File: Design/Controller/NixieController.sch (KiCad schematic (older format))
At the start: 25 parts, among them J1 Conn_01x12_Female, J2 Conn_01x12_Female, J3 Conn_01x12_Female, J4 Conn_01x12_Female, J5 Conn_01x12_Female, J6 Conn_01x12_Female, J7 Jack-DC, J8 Conn_01x02_Male, J9 Conn_01x06_Male, U1 ATtiny85-20SU, U10 74HC595, U11 74HC595, U12 74HC595, U2 DS1307Z+, U5 74HC595, U6 74HC595, U7 74HC595, U8 74HC595, U9 74HC595, Y1 32.768kHz

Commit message: Add part numbers to symbols in NixieController schematic for BOM
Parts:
- C7, C8: Digikey # (none) -> 1276-1007-6-ND; Manufacturer (none) -> SAMSUNG
- J7: Digikey # (none) -> 2092-KLDX-0202-A-ND; Manufacturer (none) -> KYCON
- R1, R2: Digikey # (none) -> 311-4.7KARDKR-ND; Manufacturer (none) -> YAGEO
- U1: Digikey # (none) -> ATTINY85-20SURDKR-ND; Manufacturer (none) -> MICROCHIP
- U10, U11, U12, U5, U6, U7, U8, U9: Digikey # (none) -> 1727-2821-6-ND; Manufacturer (none) -> NEXPERIA
- U2: Digikey # (none) -> DS1307Z+T&RDKR-ND; Manufacturer (none) -> MAXIM
- Y1: Digikey # (none) -> SER4103DKR-ND; Manufacturer (none) -> EPSON
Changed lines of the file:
@@
 F 1 "Jack-DC" H 2757 7184 50  0000 C CNN
 F 2 "Connector_BarrelJack:BarrelJack_Horizontal" H 2750 6910 50  0001 C CNN
-F 3 "~" H 2750 6910 50  0001 C CNN
+F 3 "KLDX-0202-A" H 2750 6910 50  0001 C CNN
+F 4 "2092-KLDX-0202-A-ND" H 2700 6950 50  0001 C CNN "Digikey #"
+F 5 "KYCON" H 2700 6950 50  0001 C CNN "Manufacturer"
 	1    2700 6950
 	1    0    0    -1
@@
 F 1 "ATtiny85-20SU" H 1171 1355 50  0000 R CNN
 F 2 "Package_SO:SOIC-8_5.275x5.275mm_P1.27mm" H 1700 1400 50  0001 C CIN
-F 3 "http://ww1.microchip.com/downloads/en/DeviceDoc/atmel-2586-avr-8-bit-microcontroller-attiny25-attiny45-attiny85_datasheet.pdf" H 1700 1400 50  0001 C CNN
+F 3 "ATTINY85-20SUR" H 1700 1400 50  0001 C CNN
+F 4 "ATTINY85-20SURDKR-ND" H 1700 1400 50  0001 C CNN "Digikey #"
+F 5 "MICROCHIP" H 1700 1400 50  0001 C CNN "Manufacturer"
 	1    1700 1400
 	1    0    0    -1
@@
 F 1 "74HC595" H 1750 3850 50  0000 C CNN
 F 2 "Package_SO:SOIC-16_3.9x9.9mm_P1.27mm" H 1550 3300 50  0001 C CNN
-F 3 "http://www.ti.com/lit/ds/symlink/sn74hc595.pdf" H 1550 3300 50  0001 C CNN
+F 3 "74HC595D,118" H 1550 3300 50  0001 C CNN
+F 4 "1727-2821-6-ND" H 1550 3300 50  0001 C CNN "Digikey #"
+F 5 "NEXPERIA" H 1550 3300 50  0001 C CNN "Manufacturer"
 	1    1550 3300
 	1    0    0    -1
@@
 F 1 "74HC595" H 3350 3850 50  0000 C CNN
 F 2 "Package_SO:SOIC-16_3.9x9.9mm_P1.27mm" H 3150 3300 50  0001 C CNN
-F 3 "http://www.ti.com/lit/ds/symlink/sn74hc595.pdf" H 3150 3300 50  0001 C CNN
+F 3 "74HC595D,118" H 3150 3300 50  0001 C CNN
+F 4 "1727-2821-6-ND" H 3150 3300 50  0001 C CNN "Digikey #"
+F 5 "NEXPERIA" H 3150 3300 50  0001 C CNN "Manufacturer"
 	1    3150 3300
 	1    0    0    -1
@@
 F 1 "74HC595" H 4950 3850 50  0000 C CNN
 F 2 "Package_SO:SOIC-16_3.9x9.9mm_P1.27mm" H 4750 3300 50  0001 C CNN
-F 3 "http://www.ti.com/lit/ds/symlink/sn74hc595.pdf" H 4750 3300 50  0001 C CNN
+F 3 "74HC595D,118" H 4750 3300 50  0001 C CNN
+F 4 "1727-2821-6-ND" H 4750 3300 50  0001 C CNN "Digikey #"
+F 5 "NEXPERIA" H 4750 3300 50  0001 C CNN "Manufacturer"
 	1    4750 3300
 	1    0    0    -1
@@
 F 1 "74HC595" H 6550 3850 50  0000 C CNN
 F 2 "Package_SO:SOIC-16_3.9x9.9mm_P1.27mm" H 6350 3300 50  0001 C CNN
-F 3 "http://www.ti.com/lit/ds/symlink/sn74hc595.pdf" H 6350 3300 50  0001 C CNN
+F 3 "74HC595D,118" H 6350 3300 50  0001 C CNN
+F 4 "1727-2821-6-ND" H 6350 3300 50  0001 C CNN "Digikey #"
+F 5 "NEXPERIA" H 6350 3300 50  0001 C CNN "Manufacturer"
 	1    6350 3300
 	1    0    0    -1
@@
 F 1 "74HC595" H 1750 5750 50  0000 C CNN
 F 2 "Package_SO:SOIC-16_3.9x9.9mm_P1.27mm" H 1550 5200 50  0001 C CNN
-F 3 "http://www.ti.com/lit/ds/symlink/sn74hc595.pdf" H 1550 5200 50  0001 C CNN
+F 3 "74HC595D,118" H 1550 5200 50  0001 C CNN
+F 4 "1727-2821-6-ND" H 1550 5200 50  0001 C CNN "Digikey #"
+F 5 "NEXPERIA" H 1550 5200 50  0001 C CNN "Manufacturer"
 	1    1550 5200
 	1    0    0    -1
@@
 F 1 "74HC595" H 3350 5750 50  0000 C CNN
 F 2 "Package_SO:SOIC-16_3.9x9.9mm_P1.27mm" H 3150 5200 50  0001 C CNN
-F 3 "http://www.ti.com/lit/ds/symlink/sn74hc595.pdf" H 3150 5200 50  0001 C CNN
+F 3 "74HC595D,118" H 3150 5200 50  0001 C CNN
+F 4 "1727-2821-6-ND" H 3150 5200 50  0001 C CNN "Digikey #"
+F 5 "NEXPERIA" H 3150 5200 50  0001 C CNN "Manufacturer"
 	1    3150 5200
 	1    0    0    -1
@@
 F 1 "74HC595" H 4950 5750 50  0000 C CNN
 F 2 "Package_SO:SOIC-16_3.9x9.9mm_P1.27mm" H 4750 5200 50  0001 C CNN
-F 3 "http://www.ti.com/lit/ds/symlink/sn74hc595.pdf" H 4750 5200 50  0001 C CNN
+F 3 "74HC595D,118" H 4750 5200 50  0001 C CNN
+F 4 "1727-2821-6-ND" H 4750 5200 50  0001 C CNN "Digikey #"
+F 5 "NEXPERIA" H 4750 5200 50  0001 C CNN "Manufacturer"
 	1    4750 5200
 	1    0    0    -1
@@
 F 1 "74HC595" H 6550 5750 50  0000 C CNN
 F 2 "Package_SO:SOIC-16_3.9x9.9mm_P1.27mm" H 6350 5200 50  0001 C CNN
-F 3 "http://www.ti.com/lit/ds/symlink/sn74hc595.pdf" H 6350 5200 50  0001 C CNN
+F 3 "74HC595D,118" H 6350 5200 50  0001 C CNN
+F 4 "1727-2821-6-ND" H 6350 5200 50  0001 C CNN "Digikey #"
+F 5 "NEXPERIA" H 6350 5200 50  0001 C CNN "Manufacturer"
 	1    6350 5200
 	1    0    0    -1
@@
 F 1 "4.7K" H 5020 1155 50  0000 L CNN
 F 2 "Resistor_SMD:R_0805_2012Metric" V 4880 1200 50  0001 C CNN
-F 3 "~" H 4950 1200 50  0001 C CNN
+F 3 "RC0805JR-074K7L" H 4950 1200 50  0001 C CNN
+F 4 "311-4.7KARDKR-ND" H 4950 1200 50  0001 C CNN "Digikey #"
+F 5 "YAGEO" H 4950 1200 50  0001 C CNN "Manufacturer"
 	1    4950 1200
 	1    0    0    -1
@@
 F 1 "4.7K" H 4720 1155 50  0000 L CNN
 F 2 "Resistor_SMD:R_0805_2012Metric" V 4580 1200 50  0001 C CNN
-F 3 "~" H 4650 1200 50  0001 C CNN
+F 3 "RC0805JR-074K7L" H 4650 1200 50  0001 C CNN
+F 4 "311-4.7KARDKR-ND" H 4650 1200 50  0001 C CNN "Digikey #"
+F 5 "YAGEO" H 4650 1200 50  0001 C CNN "Manufacturer"
 	1    4650 1200
 	1    0    0    -1
@@
 F 1 "DS1307Z+" H 6700 1250 50  0000 L CNN
 F 2 "Package_SO:SOIC-8_3.9x4.9mm_P1.27mm" H 6250 1000 50  0001 C CNN
-F 3 "https://datasheets.maximintegrated.com/en/ds/DS1307.pdf" H 6250 1500 50  0001 C CNN
+F 3 "DS1307Z+T&R" H 6250 1500 50  0001 C CNN
+F 4 "DS1307Z+T&RDKR-ND" H 6250 1500 50  0001 C CNN "Digikey #"
+F 5 "MAXIM" H 6250 1500 50  0001 C CNN "Manufacturer"
 	1    6250 1500
 	1    0    0    -1
@@
 F 1 "32.768kHz" V 5650 1150 50  0000 L CNN
 F 2 "Crystal:Crystal_SMD_3215-2Pin_3.2x1.5mm" H 5550 1650 50  0001 C CNN
-F 3 "~" H 5550 1650 50  0001 C CNN
+F 3 "FC-135 32.7680KA-A5" H 5550 1650 50  0001 C CNN
+F 4 "SER4103DKR-ND" H 5550 1650 50  0001 C CNN "Digikey #"
+F 5 "EPSON" H 5550 1650 50  0001 C CNN "Manufacturer"
 	1    5550 1650
 	0    1    1    0
@@
 F 1 "100nF" H 3065 2055 50  0000 L CNN
 F 2 "Capacitor_SMD:C_0805_2012Metric" H 2988 1950 50  0001 C CNN
-F 3 "~" H 2950 2100 50  0001 C CNN
+F 3 "CL21F104ZBCNNNC" H 2950 2100 50  0001 C CNN
+F 4 "1276-1007-6-ND" H 2950 2100 50  0001 C CNN "Digikey #"
+F 5 "SAMSUNG" H 2950 2100 50  0001 C CNN "Manufacturer"
 	1    2950 2100
 	1    0    0    -1
@@
 F 1 "100nF" H 3565 2055 50  0000 L CNN
 F 2 "Capacitor_SMD:C_0805_2012Metric" H 3488 1950 50  0001 C CNN
-F 3 "~" H 3450 2100 50  0001 C CNN
+F 3 "CL21F104ZBCNNNC" H 3450 2100 50  0001 C CNN
+F 4 "1276-1007-6-ND" H 3450 2100 50  0001 C CNN "Digikey #"
+F 5 "SAMSUNG" H 3450 2100 50  0001 C CNN "Manufacturer"
 	1    3450 2100
 	1    0    0    -1

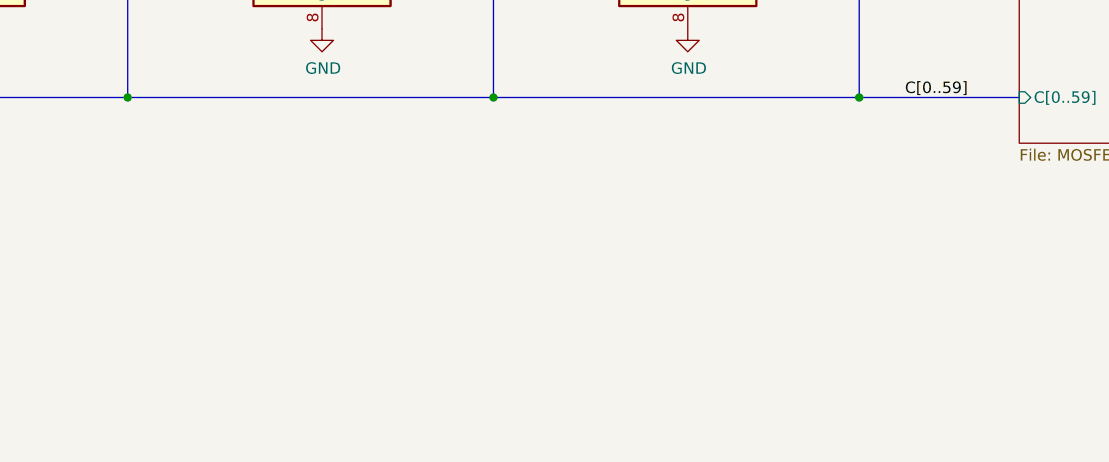
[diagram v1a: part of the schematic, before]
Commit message: Add license notice to all human readable files
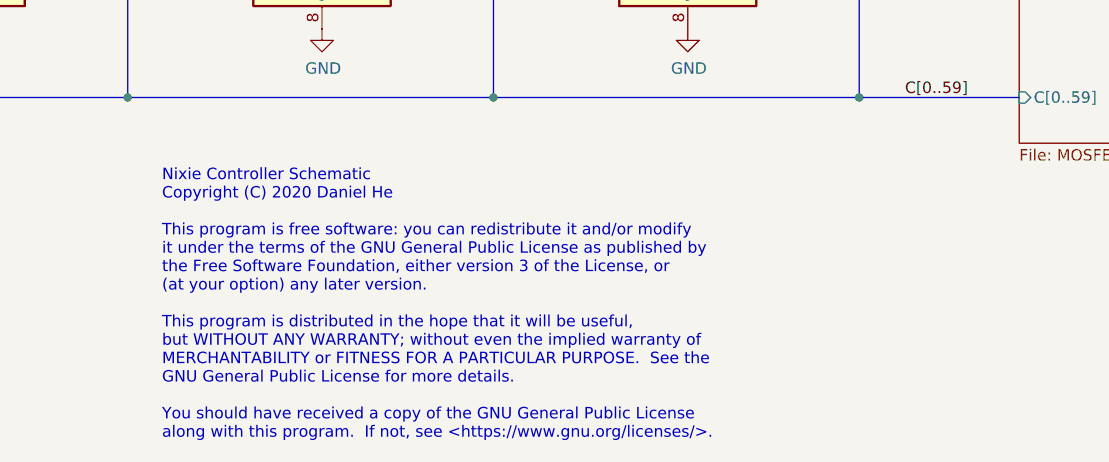
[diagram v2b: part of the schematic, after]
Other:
- note added: "Nixie Controller Schematic\nCopyright (C) 2020 Daniel He\n\nThis program is free software: you can redistribute it and/or modify\nit under the terms of the GNU General Public License as published by\nthe Free Software Foundation, either version 3 of the License, or\n(at your option) any later version.\n\nThis program is distributed in the hope that it will be useful,\nbut WITHOUT ANY WARRANTY; wi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"
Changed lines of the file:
@@
 Wire Bus Line
 	2300 3000 2300 6200
+Text Notes 4050 7700 0    50   ~ 0
+Nixie Controller Schematic\nCopyright (C) 2020 Daniel He\n\nThis program is free software: you can redistribute it and/or modify\nit under the terms of the GNU General Public License as published by\nthe Free Software Foundation, either version 3 of the License, or\n(at your option) any later version.\n\nThis program is distributed in the hope that it will be useful,\nbut WITHOUT ANY WARRANTY; without even the implied warranty of\nMERCHANTABILITY or FITNESS FOR A PARTICULAR PURPOSE.  See the\nGNU General Public License for more details.\n\nYou should have received a copy of the GNU General Public License\nalong with this program.  If not, see <https://www.gnu.org/licenses/>.
 $EndSCHEMATC
